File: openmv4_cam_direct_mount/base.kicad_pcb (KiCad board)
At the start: 4 copper layers, 36 x 34 mm, 58 parts, among them J5 XF2M-1015-1A, Q1 BSS138, Q2 Si2301BDS, U1 STM32H743VIT6, U2 OV7725, U5 TPS731XX, U8 PAM2305AABADJ, X1 MF-CON-MICROUSB-RIGHT, X2 USD-1040310811, Y1 7S-12.000MAHE-T

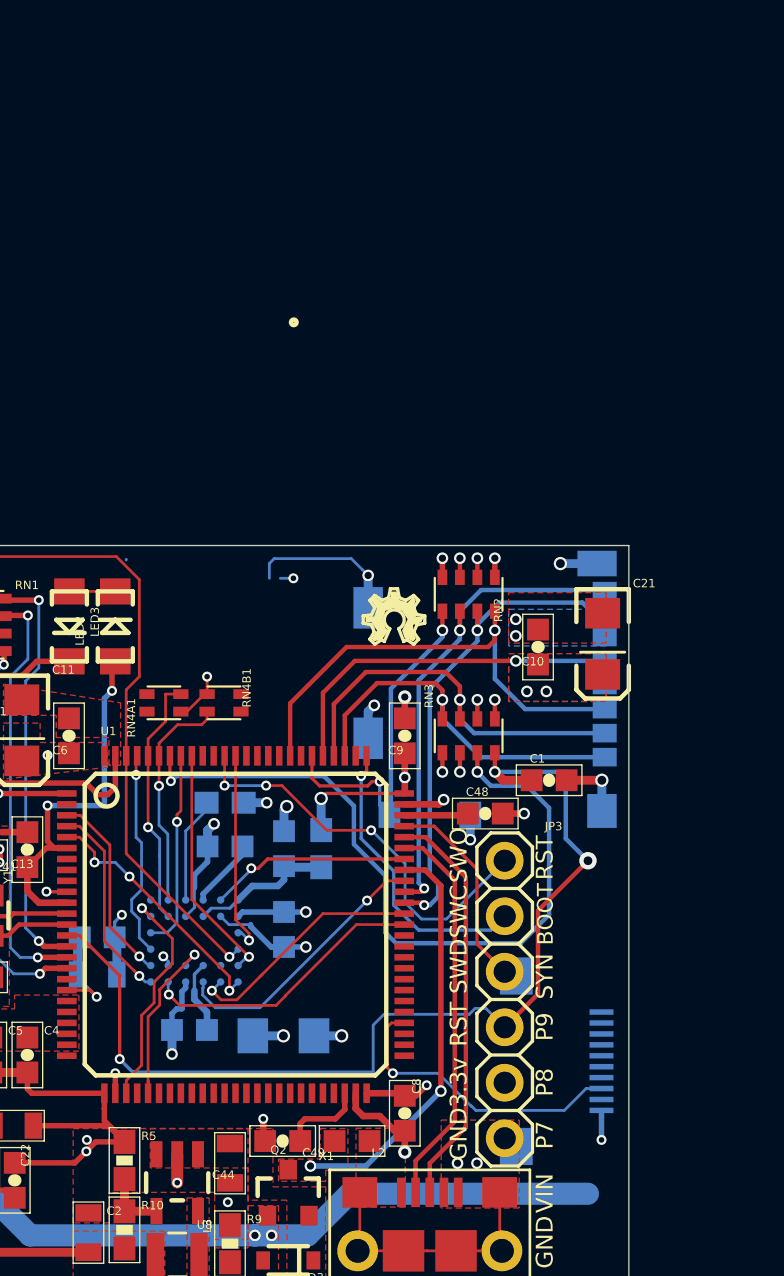
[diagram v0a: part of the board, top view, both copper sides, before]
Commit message: Added connector
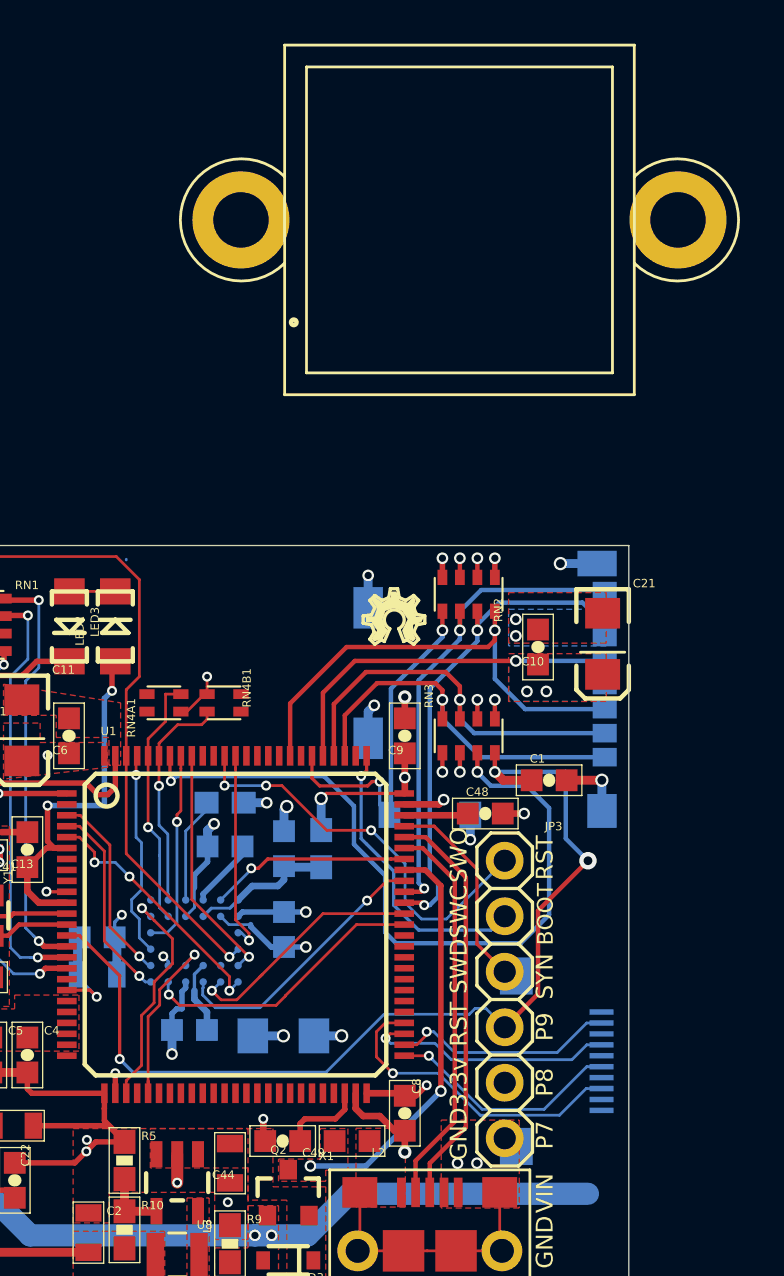
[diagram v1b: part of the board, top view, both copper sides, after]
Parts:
- added LM1: LENSMOUNT20MM, openmv3:LENSMOUNT-20MM, F.Cu at (158.8, 78.6)
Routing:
- net /SPI2_MISO: track 0.00 -> 11.5 mm, vias 0 -> 1
- net /SPI2_NSS: track 0.00 -> 10.9 mm, vias 0 -> 1
- net /SPI2_SCLK: track 0.00 -> 10.3 mm, vias 0 -> 1
- net GND: track 83.5 -> 77.9 mm
- net VCC: track 62.3 -> 60.4 mm, vias 24 -> 22
- net /NRST: track 47.3 -> 46.1 mm
- net /SPI2_MOSI: track 13.7 -> 14.5 mm

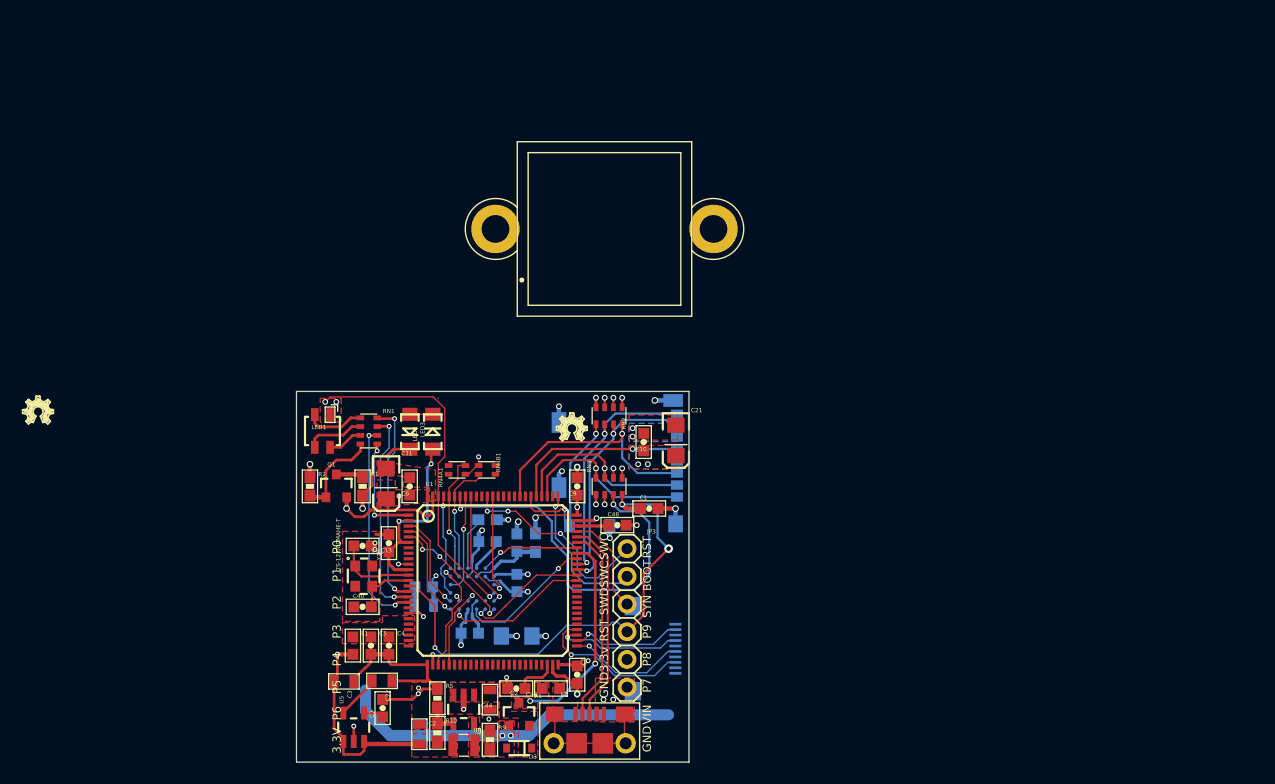
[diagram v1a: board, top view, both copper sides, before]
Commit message: Made basev2 with more clearance for camera to SD card
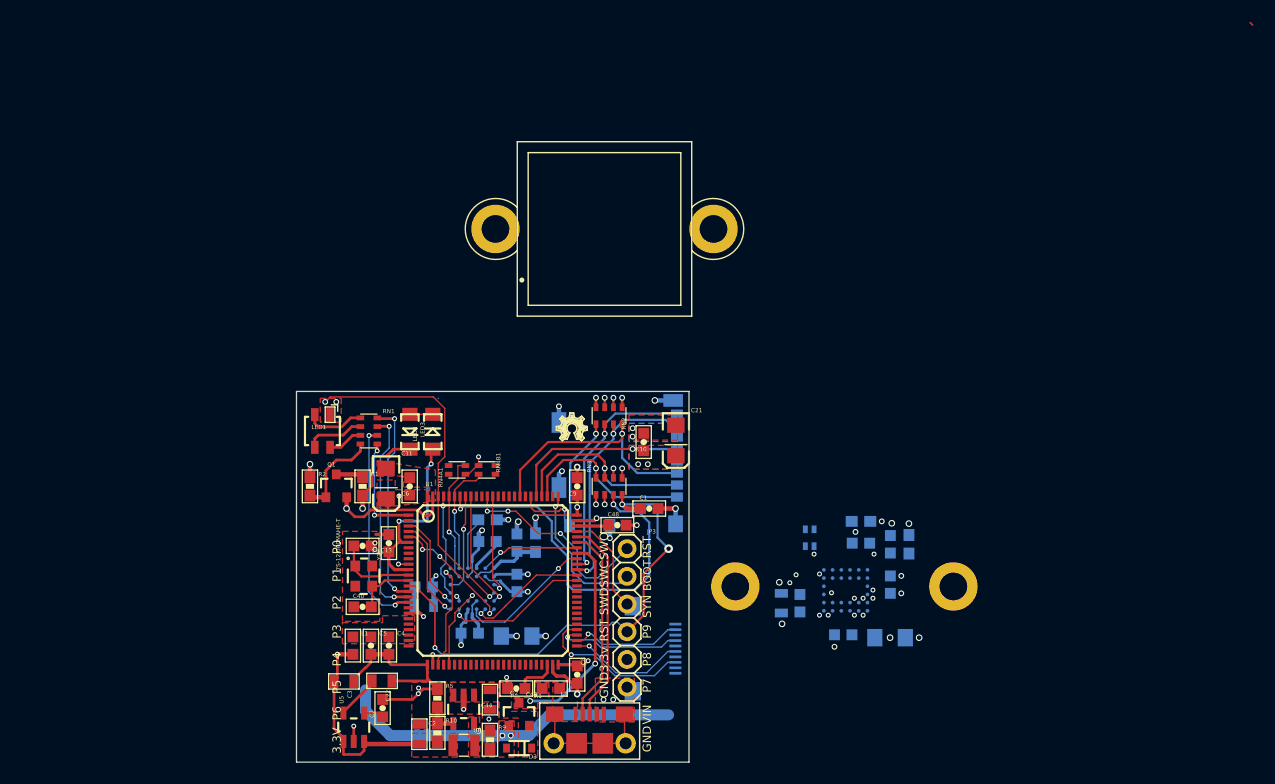
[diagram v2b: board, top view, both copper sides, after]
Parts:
- removed the LOGO1 at (105.4, 96.5)
- added C12: 47uF, openmv3:EIA3216, B.Cu at (184.9, 116.1)
- added C15: 0.1uF, openmv3:0603-CAP, B.Cu at (180.6, 115.8)
- added C16: 0.1uF, openmv3:0603-CAP, B.Cu at (185.0, 111.2)
- added C17: 0.1uF, openmv3:0603-CAP, B.Cu at (182.3, 107.4)
- added C18: 4.7uF, openmv3:0603-CAP, B.Cu at (185.0, 107.5)
- added C19: 0.1uF, openmv3:0603-CAP, B.Cu at (176.7, 112.9)
- added C20: 22uF, openmv3:0805, B.Cu at (142.2, 113.1)
- added LM1: LENSMOUNT20MM, openmv3:LENSMOUNT-20MM, B.Cu at (180.8, 111.4)
- added R3: 10k, openmv3:0603-RES, B.Cu at (182.3, 105.4)
- added R4: 4.7R, openmv3:0603-RES, B.Cu at (186.7, 107.5)
- added RN4: 4.7K, openmv3:EXBV4V, B.Cu at (177.6, 106.9)
- added U2: OV7725, openmv3:CSP2-28, B.Cu at (180.9, 111.7)
- moved C20 32.8 mm to (175.0, 112.9), turned to 90 degrees
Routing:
- net /DCMI_HSYNC: track 10.5 -> 9.87 mm, vias 1 -> 2
- net /DCMI_D3: vias 2 -> 4
- net VCC: vias 22 -> 26
- net Net-(C16-Pad1): vias 1 -> 2
- net GND: vias 32 -> 39
- net /DCMI_RST: vias 1 -> 2
- net /DCMI_PWDN: vias 1 -> 2
- net /DCMI_PCLK: vias 1 -> 2
- net /DCMI_D7: vias 3 -> 4
- net /DCMI_D6: vias 1 -> 2
- net /DCMI_D5: vias 1 -> 2
- net /DCMI_D4: vias 1 -> 2
- net /DCMI_D1: vias 1 -> 2
- net /DCMI_D0: vias 1 -> 2
- net /DCMI_CLK: vias 1 -> 2
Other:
- net class 2 removed
- net class Default: trace_width 0.127 -> 0.25; via_dia 0.457 -> 0.8; via_drill 0.254 -> 0.4

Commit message: Added pwr enable, fixed reg
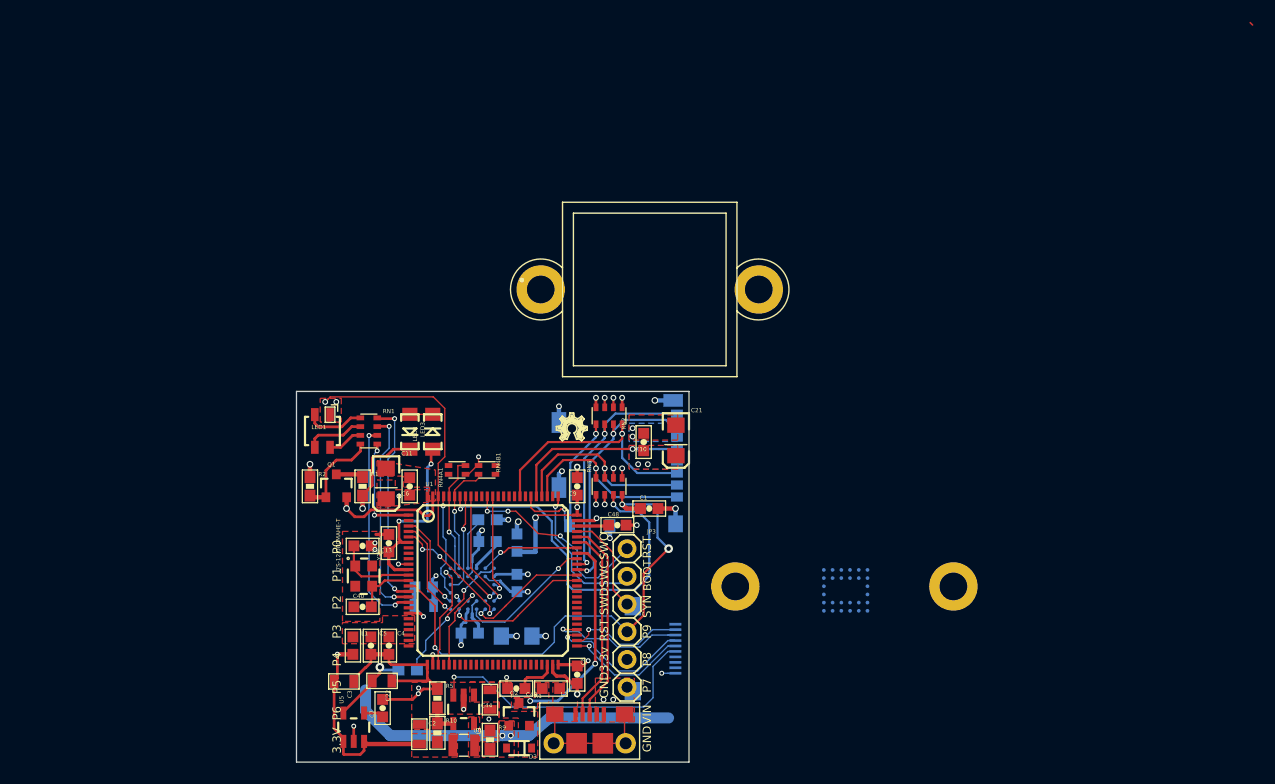
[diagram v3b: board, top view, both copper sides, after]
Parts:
- removed the C12 at (184.9, 116.1)
- removed the C15 at (180.6, 115.8)
- removed the C16 at (185.0, 111.2)
- removed the C17 at (182.3, 107.4)
- removed the C18 at (185.0, 107.5)
- removed the C19 at (176.7, 112.9)
- removed the C20 at (175.0, 112.9)
- removed the R3 at (182.3, 105.4)
- removed the R4 at (152.4, 107.4)
- removed the R4 at (186.7, 107.5)
- removed RN4: 4.7K, openmv3:EXBV4V
- added R4: 0, base:0603-RES, B.Cu at (140.7, 119.0)
- moved LM1 6.93 mm to (162.9, 84.2)
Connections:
- C18 pad 1: Net-(C18-Pad1) -> VCC
- J5 pad 10: /PWR_EN -> Net-(J5-Pad10)
- J5 pad 3: /SPI2_MOSI -> Net-(J5-Pad3)
- J5 pad 5: /SPI2_NSS -> /PWR_EN
- J5 pad 6: Net-(J5-Pad6) -> /SPI2_NSS
- J5 pad 8: Net-(J5-Pad8) -> /SPI2_MOSI
- U2 pad A1: Net-(C18-Pad1) -> Net-(R4-Pad2)
- U2 pad B3: Net-(C18-Pad1) -> Net-(R4-Pad2)
- U8 pad 3: RAW -> /PWR_EN
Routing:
- net /PWR_EN: track 0.00 -> 26.9 mm, vias 0 -> 1
- net Net-(R4-Pad2): track 0.00 -> 12.8 mm, vias 0 -> 2
- net Net-(C18-Pad1): track 6.74 -> 0.00 mm
- net VCC: track 60.4 -> 65.4 mm, vias 26 -> 23
- net VDDA: track 4.05 -> 7.39 mm, vias 0 -> 1
- net /SPI2_MISO: track 11.4 -> 13.4 mm
- net /NRST: track 46.1 -> 47.4 mm
- net /SPI2_MOSI: track 14.5 -> 13.4 mm
- net /SPI2_NSS: track 10.9 -> 11.4 mm
- net /SPI2_SCLK: track 10.3 -> 10.8 mm
- net /DCMI_D3: vias 4 -> 2
- net /DCMI_HSYNC: vias 2 -> 1
- net Net-(C16-Pad1): vias 2 -> 1
- net GND: vias 39 -> 32
- net /DCMI_RST: vias 2 -> 1
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
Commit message: Fixed clearance issue
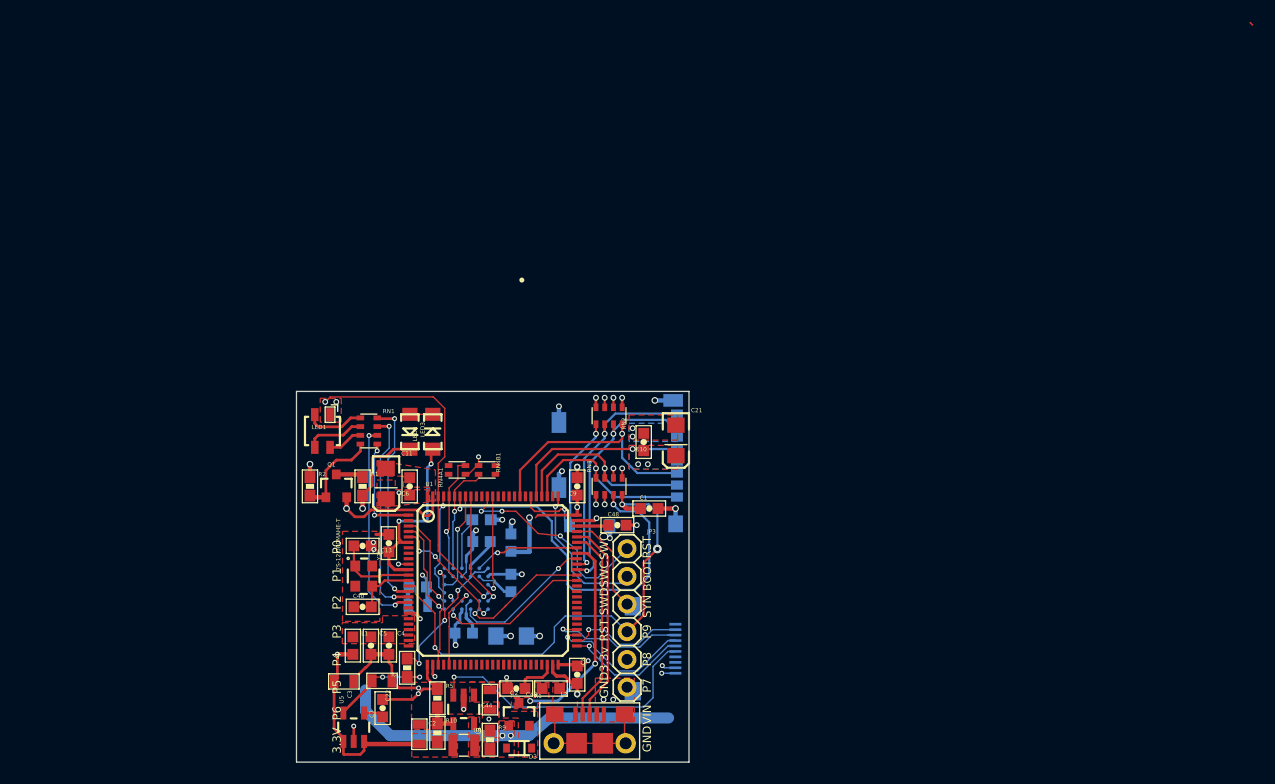
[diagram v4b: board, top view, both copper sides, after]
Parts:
- removed LM1 (x2): LENSMOUNT20MM, openmv3:LENSMOUNT-20MM
- removed LOGO1: OSHW_LOGO_FILLX0100-NT, base:OSHW_FILLX100_NOTEXT
- removed the U2 at (146.6, 111.6)
- removed the U2 at (180.9, 111.7)
- added U2: OV7725, openmv3:CSP2-28, B.Cu at (146.1, 111.6)
- R4: moved to F.Cu
- moved C15 0.55 mm to (145.8, 115.7)
- moved C16 0.55 mm to (150.2, 111.1)
- moved C17 0.55 mm to (147.5, 107.3)
- moved C18 0.55 mm to (150.2, 107.4)
- moved C19 0.55 mm to (141.6, 111.4)
- moved C20 0.55 mm to (141.6, 113.1)
- moved R3 0.55 mm to (147.5, 105.3)
- moved C12 0.50 mm to (150.2, 115.9)
- moved R4 0.21 mm to (140.7, 118.8), turned to 90 degrees
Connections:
- J5 pad 7: /SPI2_MISO -> Net-(J5-Pad7)
- J5 pad 9: /SPI2_SCLK -> Net-(J5-Pad9)
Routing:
- net VDDA: track 7.39 -> 9.69 mm, vias 1 -> 2
- net /NRST: track 47.4 -> 46.1 mm
- net GND: track 77.9 -> 76.8 mm, vias 32 -> 33
- net /SPI3_SCLK/TRACESWO: track 18.7 -> 19.5 mm
- net /DCMI_D0: track 13.1 -> 13.9 mm
- net /DCMI_CLK: track 12.6 -> 13.1 mm
- net /DCMI_D1: track 11.4 -> 11.9 mm
- net /DCMI_HSYNC: track 9.87 -> 9.34 mm
- net /DCMI_RST: track 9.21 -> 9.71 mm
- net Net-(R4-Pad2): track 12.8 -> 13.1 mm, vias 2 -> 3
- net Net-(C16-Pad1): track 5.03 -> 4.66 mm, vias 1 -> 0

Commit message: fab cleanup finished
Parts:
- added R6: 0, base:0603-RES, F.Cu at (164.0, 124.1)
- added R7: 0, base:0603-RES, F.Cu at (164.0, 122.4)
- moved C21 0.44 mm to (164.9, 98.0)
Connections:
- J5 pad 1: VCC -> Net-(J5-Pad1)
- J5 pad 4: /BATT_N -> GND
- J5 pad 5: /PWR_EN -> /SPI2_MOSI
- J5 pad 6: /SPI2_NSS -> /PWR_EN
- J5 pad 7: Net-(J5-Pad7) -> /SPI2_MISO
- J5 pad 8: /SPI2_MOSI -> /SPI2_SCLK
- J5 pad 9: Net-(J5-Pad9) -> /SPI2_NSS
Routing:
- net VCC: track 65.7 -> 32.0 mm, vias 23 -> 32
- net VIN: track 31.3 -> 0.00 mm
- net RAW: track 0.00 -> 13.5 mm, vias 0 -> 3
- net Net-(J5-Pad1): track 0.00 -> 4.69 mm, vias 0 -> 1
- net /PWR_EN: track 26.9 -> 23.3 mm, vias 1 -> 3
- net /SPI2_NSS: track 11.4 -> 13.8 mm
- net /NRST: track 46.1 -> 44.0 mm
- net /SPI2_MISO: track 13.4 -> 11.5 mm
- net /SPI2_MOSI: track 13.4 -> 12.1 mm
- net /SPI2_SCLK: track 10.8 -> 9.83 mm
- net GND: track 76.8 -> 75.9 mm, vias 33 -> 36
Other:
- board text added: "RAW"
- board text added: "VCC"
- board text added: "v00"
